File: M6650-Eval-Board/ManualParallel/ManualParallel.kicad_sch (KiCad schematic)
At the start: 12 parts, among them J1 Parallel, SW1 SW_DIP_x04, SW2 SW_DIP_x04, SW3 SW_Push, SW4 SW_Push

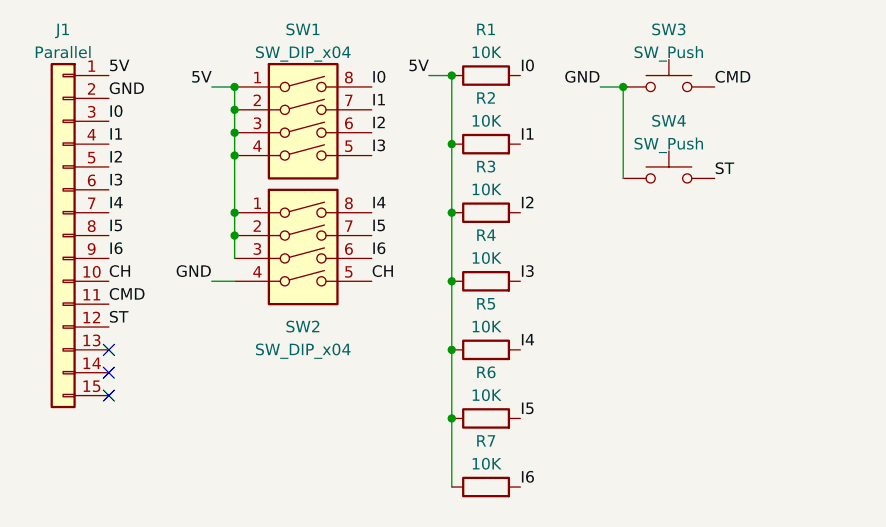
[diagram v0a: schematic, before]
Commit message: Fix a dumb error on eval board extras
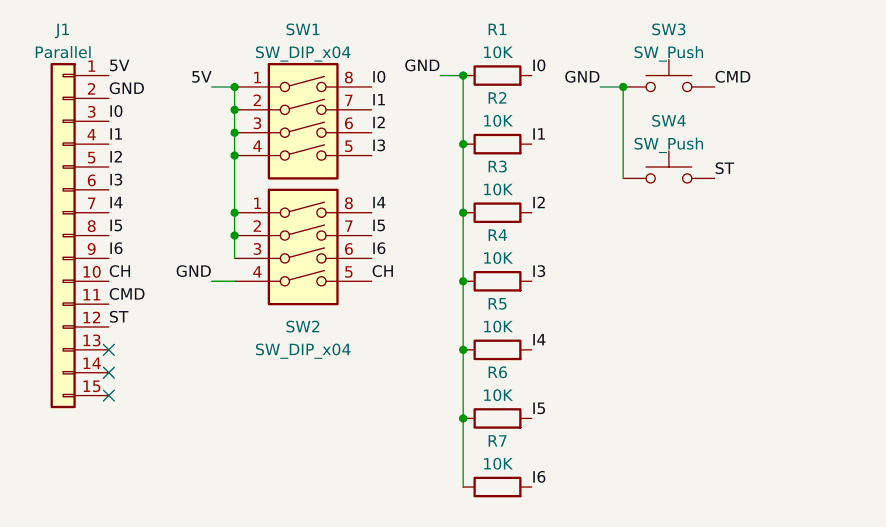
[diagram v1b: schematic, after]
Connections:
- net 5V: no longer R1.1, R2.1, R3.1, R4.1, R5.1, R6.1, R7.1
- net GND: now also R1.1, R2.1, R3.1, R4.1, R5.1, R6.1, R7.1
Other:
- moved on the sheet: R1, R2, R3, R4, R5, R6, R7

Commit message: Add debounce to manual parallel board, redo board edges and clearance rules
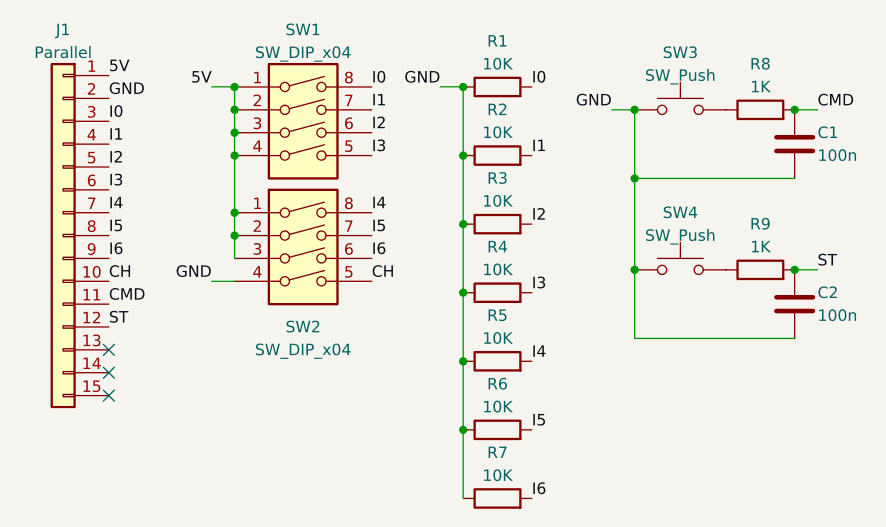
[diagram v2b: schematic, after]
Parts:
- added C1, C2: 100n, Capacitor_SMD:C_0603_1608Metric_Pad1.08x0.95mm_HandSolder, symbol Device:C
- added R8, R9: 1K, Resistor_SMD:R_0603_1608Metric_Pad0.98x0.95mm_HandSolder, symbol Device:R
- J1: footprint Connector_PinSocket_2.54mm:PinSocket_1x15_P2.54mm_Vertical -> Connector_PinHeader_2.54mm:PinHeader_1x15_P2.54mm_Vertical
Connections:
- net CMD: now also C1.1, R8.2; no longer SW3.2
- net GND: now also C1.2, C2.2
- net ST: now also C2.1, R9.2; no longer SW4.2
- new net: R9.1, SW4.2
- new net: R8.1, SW3.2
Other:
- moved on the sheet: R1, R2, R3, R4, R5, R6, R7, SW3, SW4
